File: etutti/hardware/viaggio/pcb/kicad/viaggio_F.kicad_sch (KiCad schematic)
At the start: 16 parts, among them J301 PJ-313D-6A, U301 SGTL5000XNLA3, U302 XC6206P182MR

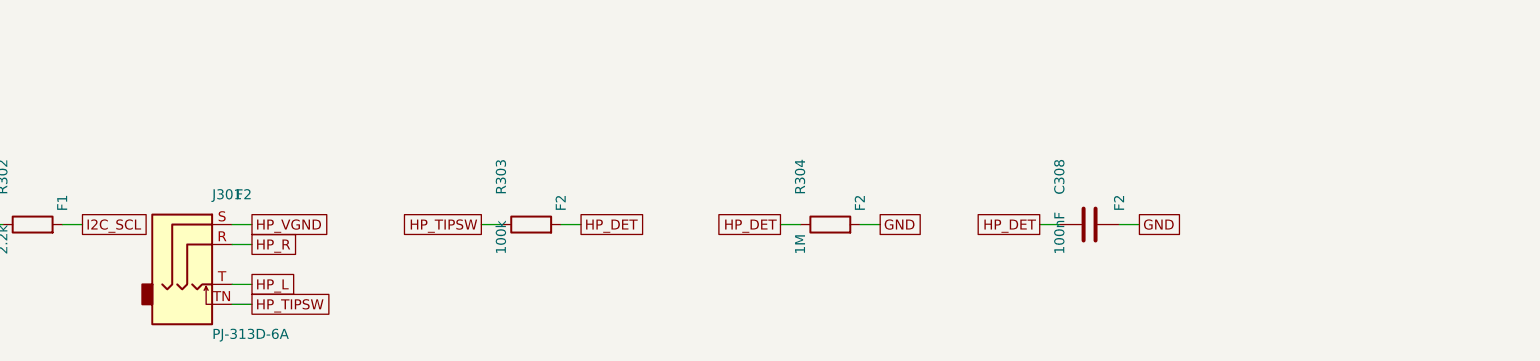
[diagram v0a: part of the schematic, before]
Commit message: eTutti Viaggio SPEC v2.1 step 3.2: placed board handed off for manual routing
- VE2a: power switch on the volume click (I1); flash W25Q64JVSSIM; both
  encoders EC11E18244A5 (the 15/15 has no stock); F2 = PJ-327A 5JJ (the
  PJ-313D-6A has no tip switch); PINOS.md and BOM updated. ERC 0/0, netlist
  check OK.
- VE2b: footprints.py writes viaggio.pretty (BGA-196 12x12 P0.8 from NXP
  figure 54, checked against rt1062_balls.json; jack; LED 1615; Gateron).
- VE2c: build_board.py builds the 246.5 x 95 board (R5 corners, M2 holes,
  silkscreen, JLC04121H-7628 stack-up, net classes, USB 90 ohm = 0.24/0.15
  per impedance.py) and places every part from viaggio_rev2.json.
- Routing: the own grid router could not close sector P (18 DRC errors),
  so J routes the board in KiCad with Freerouting. handoff_freerouting.py
  strips the tracks, links the board to the schematic, fixes 4 courtyard
  overlaps, makes In1/In2 plane layers and exports build/viaggio.dsn:
  DRC 0 errors, parity 0, 499 connections to route. Guide: ROTEAMENTO.md.

Co-Authored-By: Claude Opus 5.5 <noreply@anthropic.com>
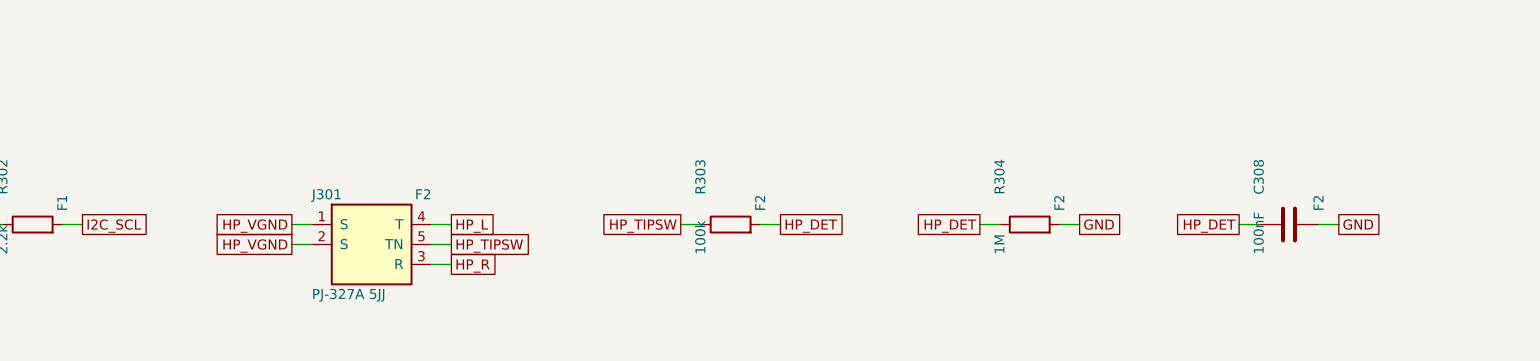
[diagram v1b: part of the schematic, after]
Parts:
- J301: value PJ-313D-6A -> PJ-327A 5JJ; footprint (none) -> viaggio:Jack_3.5mm_PJ-327A_SMD; symbol viaggio:AudioJack3_SwitchT -> viaggio:PJ-327A; LCSC C95463 -> C668605
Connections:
- net HP_L: now also J301.4 (T); no longer J301.T
- net HP_R: now also J301.3 (R); no longer J301.R
- net HP_TIPSW: now also J301.5 (TN); no longer J301.TN
- net HP_VGND: now also J301.1 (S), J301.2 (S); no longer J301.S
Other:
- moved on the sheet: C308, J301, R303, R304
